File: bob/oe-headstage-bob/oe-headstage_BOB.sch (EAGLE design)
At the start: 13 parts, among them U1 SN65LVDS1DBVR, U2 SN65LVDS2DBVR, U3 SN65LVDS1DBVR, U4 SN65LVDS1DBVR

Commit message: Minor.
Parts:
- added C10: 0.1uF, rcl:C-EUC0603
- added C9: 1nF, rcl:C-EUC0603
- added S1, S2, S3: RHD2000-CABLE-DAQ-SIDE, RHD2000_eval_board:RHD2000-CABLE-DAQ-SIDE
- added U$1: HDMI, open-ephys:HDMI
- added U5: SN65LVDS1DBVR, ti-extended:SN65LVDS1DBVR
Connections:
- net +CS renamed +CS_A
- net -CS renamed -CS_A
- net CS renamed CS_A
- new net CS_B: U5.D
- new net N$10: S1.MISO1-
- new net N$11: S1.MOSI+
- new net N$12: S1.MOSI-
- new net N$13: S1.SCLK+
- new net N$14: S1.SCLK-
- new net N$15: S1.!CS!+
- new net N$16: S1.!CS!-
- new net N$17: U$1.DATA1-
- new net N$18: U$1.DATA0+
- new net N$19: U$1.DATA0-
- new net N$20: U$1.CLOCK+
- new net N$21: U$1.CLOCK-
- new net N$5: C10.1, C9.1, U5.VCC
- new net N$6: S1.MISO2+
- new net N$7: U$1.DATA1+
- new net N$8: S1.MISO2-
- new net N$9: S1.MISO1+
- new net VDRIVE: C1.1, C2.1, C5.1, C6.1, S1.VDD, U$1.VCC, U3.VCC, U4.VCC
- net +SCLK: now also U5.Y
- net -SCLK: now also U5.Z
- net GND: now also C10.2, C9.2, S1.GND, U$1.CLOCKSHIELD, U$1.DATA0SHIELD, U$1.DATA1SHIELD, U$1.DATA2SHIELD, U5.GND
- net N$1: now also U$1.DATA2+; no longer C1.1, C2.1, U4.VCC
- net N$3: now also U$1.DATA2-; no longer C5.1, C6.1, U3.VCC

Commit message: Started differential routing on Intan BOB.
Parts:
- removed S3: RHD2000-CABLE-DAQ-SIDE, RHD2000_eval_board:RHD2000-CABLE-DAQ-SIDE
- removed U$1: HDMI, open-ephys:HDMI
- added C11, C12: 1nF, puggleboard:C_0603
- added C13: 10uF, puggleboard:C_0805
- added D_I/O: PINHD-2X8VERT, adafruit:PINHD-2X8VERT
- added R2: 100, puggleboard:R_0603
- added U6: SN65LVDS1DBVR, ti-extended:SN65LVDS1DBVR
- C1, C3, C5: value 1nF -> 0.1uF; device rcl:C-EUC0603 -> puggleboard:C_0603
- C10, C8: value 0.1uF -> 1nF; device rcl:C-EUC0603 -> puggleboard:C_0603
- C2, C4, C6, C7, C9: device rcl:C-EUC0603 -> puggleboard:C_0603
- R1: device resistor:R-US_R0603 -> puggleboard:R_0603
- U4: value SN65LVDS1DBVR -> SN65LVDS2DBVR; device ti-extended:SN65LVDS1DBVR -> ti-extended:SN65LVDS2DBVR; DIGIKEY 296-6919-1-ND -> 296-6920-1-ND
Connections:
- removed net +CS_A: U3.Y
- removed net +MISO: R1.1, U2.Y
- removed net +MOSI: U1.Y
- removed net +SCLK: U4.Y, U5.Y
- removed net -CS_A: U3.Z
- removed net -MISO: R1.2, U2.Z
- removed net -MOSI: U1.Z
- removed net -SCLK: U4.Z, U5.Z
- removed net CS_A: U3.D
- removed net CS_B: U5.D
- removed net MISO: U2.D
- removed net N$1: U$1.DATA2+
- removed net N$10: S1.MISO1-
- removed net N$11: S1.MOSI+
- removed net N$12: S1.MOSI-
- removed net N$13: S1.SCLK+
- removed net N$14: S1.SCLK-
- removed net N$15: S1.!CS!+
- removed net N$16: S1.!CS!-
- removed net N$17: U$1.DATA1-
- removed net N$18: U$1.DATA0+
- removed net N$19: U$1.DATA0-
- removed net N$2: C3.1, C4.1, U1.VCC
- removed net N$20: U$1.CLOCK+
- removed net N$21: U$1.CLOCK-
- removed net N$3: U$1.DATA2-
- removed net N$4: C7.1, C8.1, U2.VCC
- removed net N$5: C10.1, C9.1, U5.VCC
- removed net N$6: S1.MISO2+
- removed net N$7: U$1.DATA1+
- removed net N$8: S1.MISO2-
- removed net N$9: S1.MISO1+
- new net CS1: D_I/O.6, U3.D
- new net CS1_N: S1.!CS!-, U3.Z
- new net CS1_P: S1.!CS!+, U3.Y
- new net CS2: D_I/O.10, U5.D
- new net CS2_N: S2.!CS!-, U5.Z
- new net CS2_P: S2.!CS!+, U5.Y
- new net DIO_6: D_I/O.14
- new net DIO_7: D_I/O.16
- new net MISO1: D_I/O.4, U2.D
- new net MISO1_N: R1.2, S1.MISO1-, U2.Z
- new net MISO1_P: R1.1, S1.MISO1+, U2.Y
- new net MISO2: D_I/O.8, U4.D
- new net MISO2_N: R2.2, S2.MISO1-, U4.Z
- new net MISO2_P: R2.1, S2.MISO1+, U4.Y
- new net MOSI_N: S1.MOSI-, S2.MOSI-, U6.Z
- new net MOSI_P: S1.MOSI+, S2.MOSI+, U6.Y
- new net SCLK_N: S1.SCLK-, S2.SCLK-, U1.Z
- new net SCLK_P: S1.SCLK+, S2.SCLK+, U1.Y
- net GND: now also C11.2, C12.2, C13.2, D_I/O.11, D_I/O.13, D_I/O.15, D_I/O.3, D_I/O.5, D_I/O.7, D_I/O.9, S2.GND, U6.GND; no longer U$1.CLOCKSHIELD, U$1.DATA0SHIELD, U$1.DATA1SHIELD, U$1.DATA2SHIELD
- net MOSI: now also D_I/O.12, U6.D; no longer U1.D
- net SCLK: now also D_I/O.2, U1.D; no longer U4.D
- net VDRIVE: now also C10.1, C11.1, C12.1, C13.1, C3.1, C4.1, C7.1, C8.1, C9.1, D_I/O.1, S2.VDD, U1.VCC, U2.VCC, U5.VCC, U6.VCC; no longer U$1.VCC

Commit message: Working through LVDS BOB, still.
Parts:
- removed S1, S2: RHD2000-CABLE-DAQ-SIDE, RHD2000_eval_board:RHD2000-CABLE-DAQ-SIDE
- added U$1, U$2: RHD2000-CABLE-DAQ-SIDE-SINGLE, puggleboard:RHD2000-CABLE-DAQ-SIDE-SINGLE
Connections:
- net DIO_7 renamed DIO7
- removed net DIO_6: D_I/O.14
- new net DIO1: D_I/O.2
- net CS1: now also D_I/O.8; no longer D_I/O.6
- net CS1_N: now also U$1.!CS!-; no longer S1.!CS!-
- net CS1_P: now also U$1.!CS!+; no longer S1.!CS!+
- net CS2: now also D_I/O.14; no longer D_I/O.10
- net CS2_N: now also U$2.!CS!-; no longer S2.!CS!-
- net CS2_P: now also U$2.!CS!+; no longer S2.!CS!+
- net GND: now also U$1.GND, U$2.GND; no longer S1.GND, S2.GND
- net MISO1_N: now also U$1.MISO1-; no longer S1.MISO1-
- net MISO1_P: now also U$1.MISO1+; no longer S1.MISO1+
- net MISO2: now also D_I/O.10; no longer D_I/O.8
- net MISO2_N: now also U$2.MISO1-; no longer S2.MISO1-
- net MISO2_P: now also U$2.MISO1+; no longer S2.MISO1+
- net MOSI_N: now also U$1.MOSI-, U$2.MOSI-; no longer S1.MOSI-, S2.MOSI-
- net MOSI_P: now also U$1.MOSI+, U$2.MOSI+; no longer S1.MOSI+, S2.MOSI+
- net SCLK: now also D_I/O.6; no longer D_I/O.2
- net SCLK_N: now also U$1.SCLK-, U$2.SCLK-; no longer S1.SCLK-, S2.SCLK-
- net SCLK_P: now also U$1.SCLK+, U$2.SCLK+; no longer S1.SCLK+, S2.SCLK+
- net VDRIVE: now also U$1.VDD, U$2.VDD; no longer S1.VDD, S2.VDD

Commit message: Working through LVDS BOB, still.
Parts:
- added R3, R4, R5, R6, R7, R8: 0, puggleboard:R_0603
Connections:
- new net N$2: R4.1, U2.D
- new net N$3: R5.1, U3.D
- new net N$4: R6.1, U4.D
- new net N$5: R7.1, U5.D
- new net N$6: R8.1, U6.D
- new net N$7: R3.1, U1.D
- net CS1: now also R5.2; no longer U3.D
- net CS2: now also R7.2; no longer U5.D
- net MISO1: now also R4.2; no longer U2.D
- net MISO2: now also R6.2; no longer U4.D
- net MOSI: now also R8.2; no longer U6.D
- net SCLK: now also R3.2; no longer U1.D
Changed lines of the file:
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@@
 <class number="0" name="default" width="0" drill="0">
 </class>
-<class number="1" name="supply" width="0.6096" drill="0">
+<class number="1" name="supply" width="0.254" drill="0">
 </class>
 <class number="2" name="diffpair" width="0.1778" drill="0">
@@
 <part name="U$1" library="puggleboard" deviceset="RHD2000-CABLE-DAQ-SIDE-SINGLE" device=""/>
 <part name="U$2" library="puggleboard" deviceset="RHD2000-CABLE-DAQ-SIDE-SINGLE" device=""/>
+<part name="R3" library="puggleboard" deviceset="R" device="_0603" value="0"/>
+<part name="R4" library="puggleboard" deviceset="R" device="_0603" value="0"/>
+<part name="R5" library="puggleboard" deviceset="R" device="_0603" value="0"/>
+<part name="R6" library="puggleboard" deviceset="R" device="_0603" value="0"/>
+<part name="R7" library="puggleboard" deviceset="R" device="_0603" value="0"/>
+<part name="R8" library="puggleboard" deviceset="R" device="_0603" value="0"/>
 </parts>
 <sheets>
@@
 <instance part="U$1" gate="G$1" x="167.64" y="20.32" rot="R90"/>
 <instance part="U$2" gate="G$1" x="167.64" y="-43.18" rot="R90"/>
+<instance part="R3" gate="R" x="15.24" y="68.58" rot="R180"/>
+<instance part="R4" gate="R" x="15.24" y="33.02" rot="R180"/>
+<instance part="R5" gate="R" x="15.24" y="-2.54" rot="R180"/>
+<instance part="R6" gate="R" x="15.24" y="-38.1" rot="R180"/>
+<instance part="R7" gate="R" x="15.24" y="-73.66" rot="R180"/>
+<instance part="R8" gate="R" x="15.24" y="-109.22" rot="R180"/>
 </instances>
 <busses>
@@
 <net name="SCLK" class="0">
 <segment>
-<pinref part="U1" gate="A" pin="D"/>
-<wire x1="22.86" y1="68.58" x2="5.08" y2="68.58" width="0.1524" layer="91"/>
 <label x="5.08" y="68.58" size="1.778" layer="95"/>
+<wire x1="7.62" y1="68.58" x2="5.08" y2="68.58" width="0.1524" layer="91"/>
+<wire x1="7.62" y1="68.58" x2="7.62" y2="66.04" width="0.1524" layer="91"/>
+<pinref part="R3" gate="R" pin="2"/>
+<wire x1="7.62" y1="68.58" x2="10.16" y2="68.58" width="0.1524" layer="91"/>
+<junction x="7.62" y="68.58"/>
 </segment>
 <segment>
@@
 <net name="MOSI" class="0">
 <segment>
-<pinref part="U6" gate="A" pin="D"/>
-<wire x1="22.86" y1="-109.22" x2="5.08" y2="-109.22" width="0.1524" layer="91"/>
-<label x="5.08" y="-109.22" size="1.778" layer="95"/>
+<label x="2.54" y="-109.22" size="1.778" layer="95"/>
+<wire x1="2.54" y1="-109.22" x2="10.16" y2="-109.22" width="0.1524" layer="91"/>
+<pinref part="R8" gate="R" pin="2"/>
 </segment>
 <segment>
@@
 <net name="CS1" class="0">
 <segment>
-<pinref part="U3" gate="A" pin="D"/>
-<wire x1="22.86" y1="-2.54" x2="5.08" y2="-2.54" width="0.1524" layer="91"/>
-<label x="5.08" y="-2.54" size="1.778" layer="95"/>
+<label x="2.54" y="-2.54" size="1.778" layer="95"/>
+<wire x1="2.54" y1="-2.54" x2="10.16" y2="-2.54" width="0.1524" layer="91"/>
+<pinref part="R5" gate="R" pin="2"/>
 </segment>
 <segment>
@@
 <net name="MISO1" class="0">
 <segment>
-<pinref part="U2" gate="A" pin="D"/>
-<wire x1="22.86" y1="33.02" x2="5.08" y2="33.02" width="0.1524" layer="91"/>
-<label x="5.08" y="33.02" size="1.778" layer="95"/>
+<label x="2.54" y="33.02" size="1.778" layer="95"/>
+<wire x1="2.54" y1="33.02" x2="10.16" y2="33.02" width="0.1524" layer="91"/>
+<pinref part="R4" gate="R" pin="2"/>
 </segment>
 <segment>
@@
 <net name="MISO2" class="0">
 <segment>
-<pinref part="U4" gate="A" pin="D"/>
-<wire x1="22.86" y1="-38.1" x2="5.08" y2="-38.1" width="0.1524" layer="91"/>
-<label x="5.08" y="-38.1" size="1.778" layer="95"/>
+<label x="2.54" y="-38.1" size="1.778" layer="95"/>
+<wire x1="2.54" y1="-38.1" x2="10.16" y2="-38.1" width="0.1524" layer="91"/>
+<pinref part="R6" gate="R" pin="2"/>
 </segment>
 <segment>
@@
 <net name="CS2" class="0">
 <segment>
-<pinref part="U5" gate="A" pin="D"/>
-<wire x1="22.86" y1="-73.66" x2="5.08" y2="-73.66" width="0.1524" layer="91"/>
-<label x="5.08" y="-73.66" size="1.778" layer="95"/>
+<label x="2.54" y="-73.66" size="1.778" layer="95"/>
+<wire x1="2.54" y1="-73.66" x2="10.16" y2="-73.66" width="0.1524" layer="91"/>
+<pinref part="R7" gate="R" pin="2"/>
 </segment>
 <segment>
@@
 </segment>
 </net>
+<net name="N$2" class="1">
+<segment>
+<pinref part="R4" gate="R" pin="1"/>
+<pinref part="U2" gate="A" pin="D"/>
+<wire x1="20.32" y1="33.02" x2="22.86" y2="33.02" width="0.1524" layer="91"/>
+</segment>
+</net>
+<net name="N$3" class="1">
+<segment>
+<pinref part="R5" gate="R" pin="1"/>
+<pinref part="U3" gate="A" pin="D"/>
+<wire x1="20.32" y1="-2.54" x2="22.86" y2="-2.54" width="0.1524" layer="91"/>
+</segment>
+</net>
+<net name="N$4" class="1">
+<segment>
+<pinref part="R6" gate="R" pin="1"/>
+<pinref part="U4" gate="A" pin="D"/>
+<wire x1="20.32" y1="-38.1" x2="22.86" y2="-38.1" width="0.1524" layer="91"/>
+</segment>
+</net>
+<net name="N$5" class="1">
+<segment>
+<pinref part="R7" gate="R" pin="1"/>
+<pinref part="U5" gate="A" pin="D"/>
+<wire x1="20.32" y1="-73.66" x2="22.86" y2="-73.66" width="0.1524" layer="91"/>
+</segment>
+</net>
+<net name="N$6" class="1">
+<segment>
+<pinref part="R8" gate="R" pin="1"/>
+<pinref part="U6" gate="A" pin="D"/>
+<wire x1="20.32" y1="-109.22" x2="22.86" y2="-109.22" width="0.1524" layer="91"/>
+</segment>
+</net>
+<net name="N$7" class="1">
+<segment>
+<pinref part="R3" gate="R" pin="1"/>
+<pinref part="U1" gate="A" pin="D"/>
+<wire x1="20.32" y1="68.58" x2="22.86" y2="68.58" width="0.1524" layer="91"/>
+</segment>
+</net>

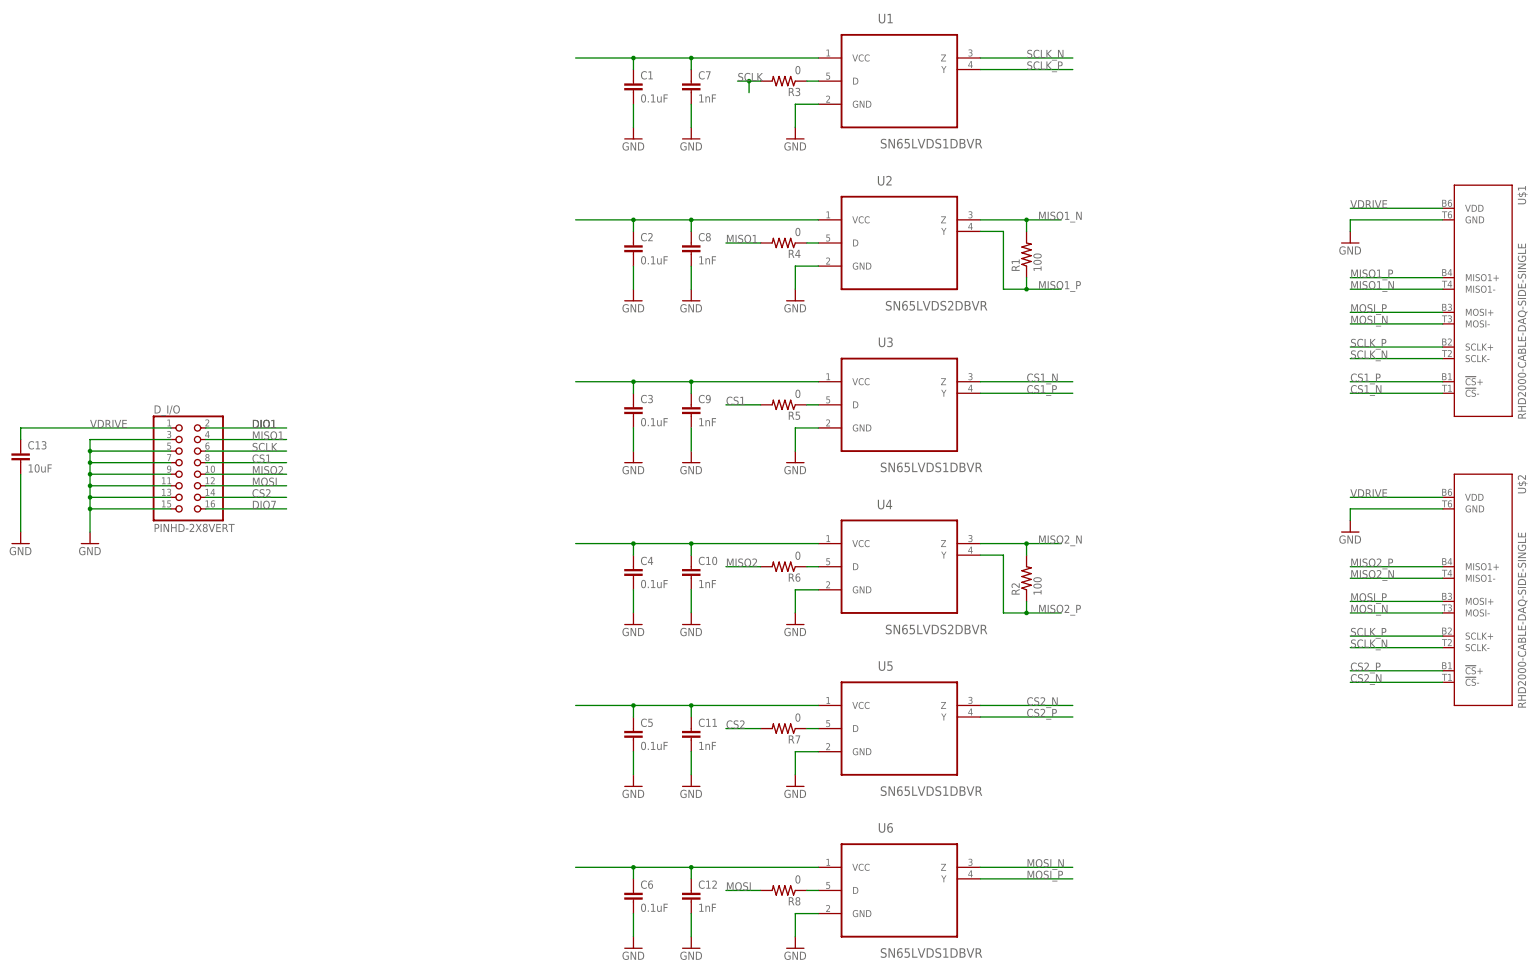
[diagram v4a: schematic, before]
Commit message: All that needs to be done is silk-screen work.
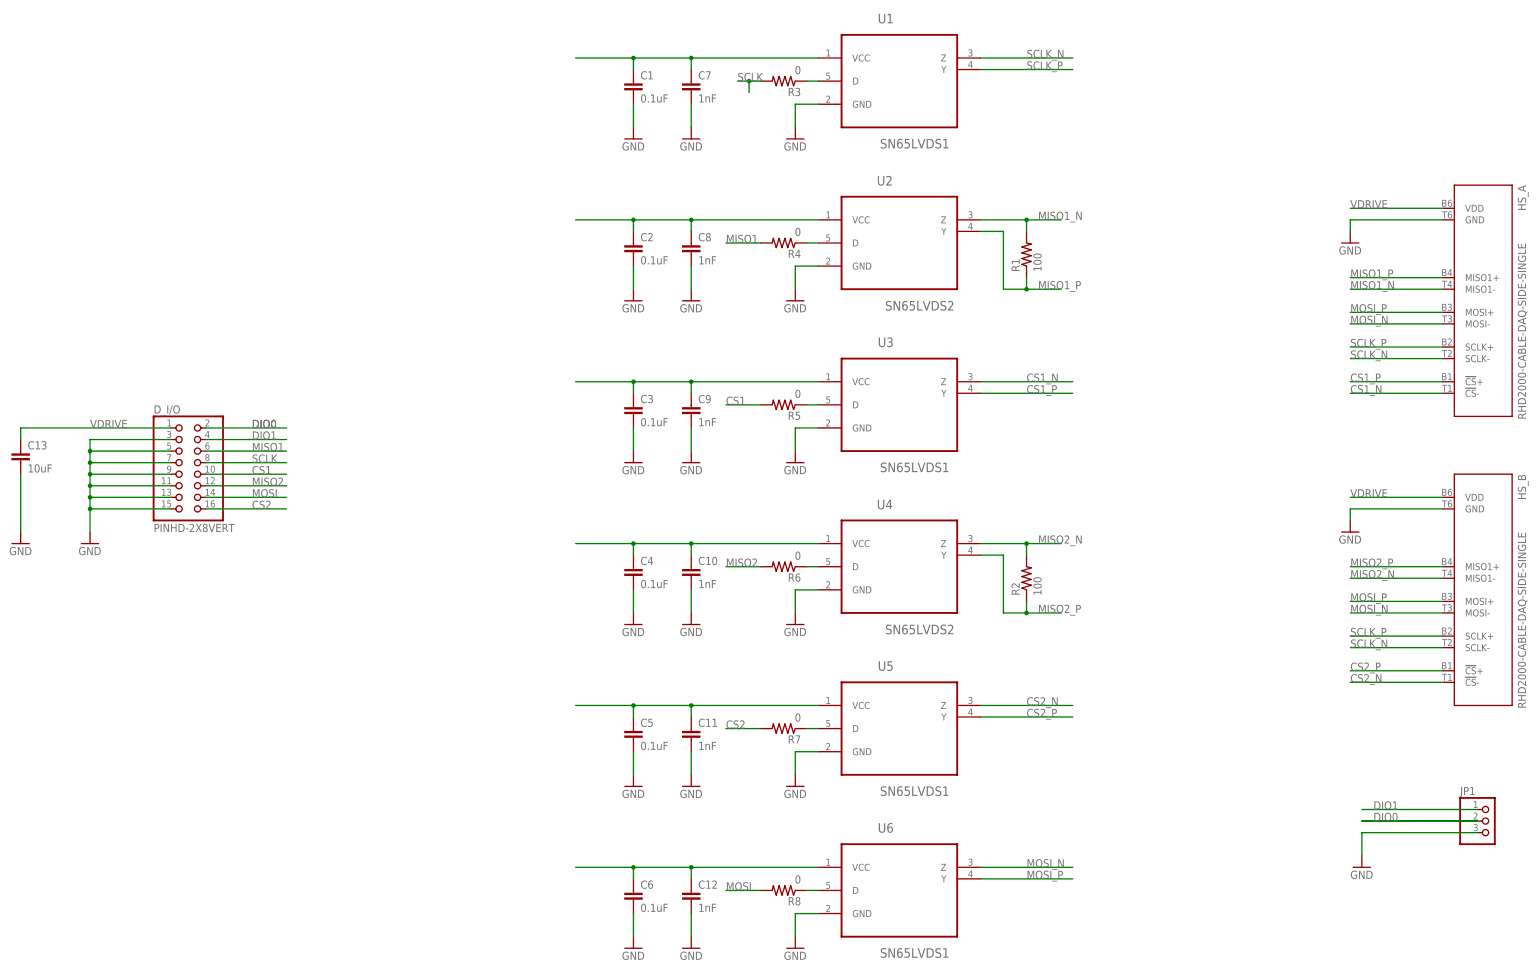
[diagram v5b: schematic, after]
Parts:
- added JP1: (no value), adafruit:PINHD-1X3
- U1, U3, U5, U6: value SN65LVDS1DBVR -> SN65LVDS1
- U2, U4: value SN65LVDS2DBVR -> SN65LVDS2
- renumbered U$1 to HS_A, U$2 to HS_B
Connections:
- removed net DIO7: D_I/O.16
- new net DIO0: D_I/O.2, JP1.2
- net CS1: now also D_I/O.10; no longer D_I/O.8
- net CS2: now also D_I/O.16; no longer D_I/O.14
- net DIO1: now also D_I/O.4, JP1.1; no longer D_I/O.2
- net GND: now also JP1.3
- net MISO1: now also D_I/O.6; no longer D_I/O.4
- net MISO2: now also D_I/O.12; no longer D_I/O.10
- net MOSI: now also D_I/O.14; no longer D_I/O.12
- net SCLK: now also D_I/O.8; no longer D_I/O.6
